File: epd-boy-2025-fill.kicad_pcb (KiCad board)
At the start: 2 copper layers, 33 x 64.5 mm, 43 parts, among them J1 FH12A-24S-0.5SH(55), Q1 SI1308EDL-T1-GE3, SW1 SW_Push, SW10 SW_SPDT, SW2 SW_Push, SW3 SW_Push, SW4 SW_Push, SW5 SW_Push, SW6 SW_Push, SW7 SW_Push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

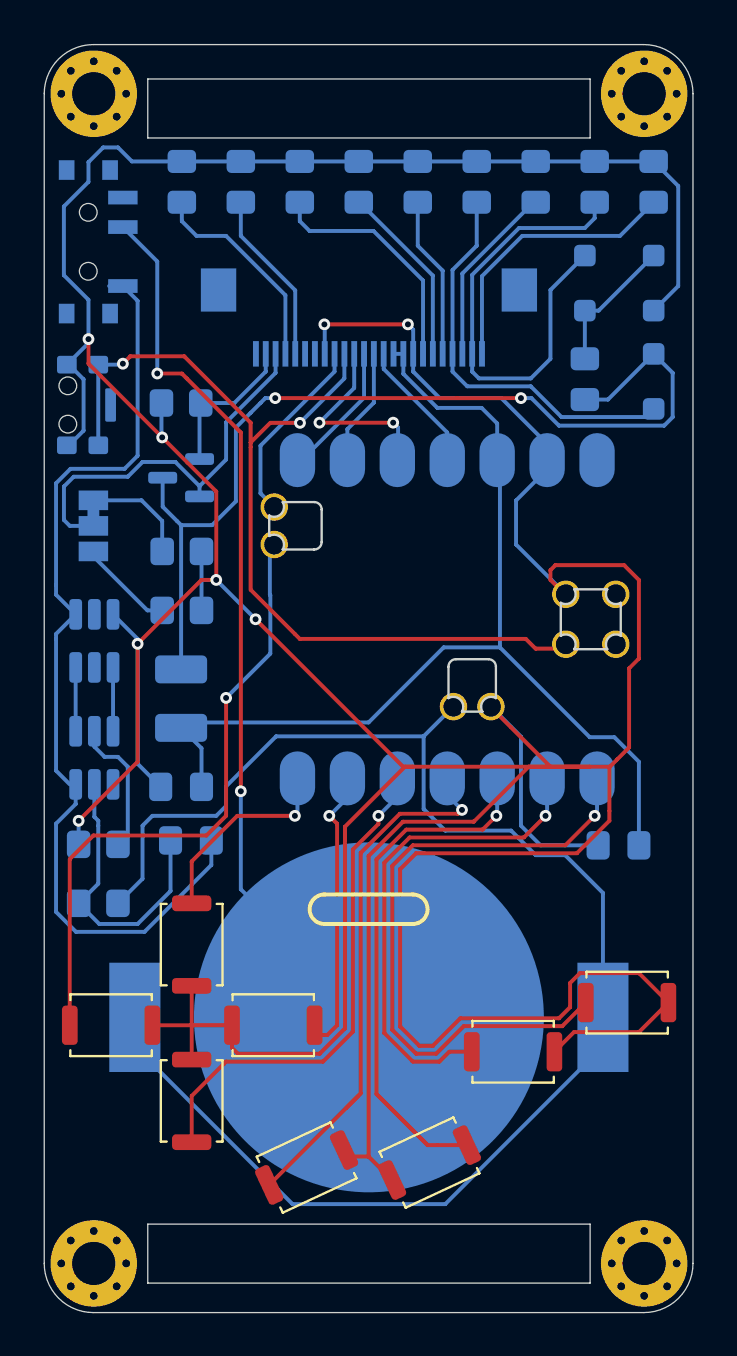
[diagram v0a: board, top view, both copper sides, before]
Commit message: Rerouted
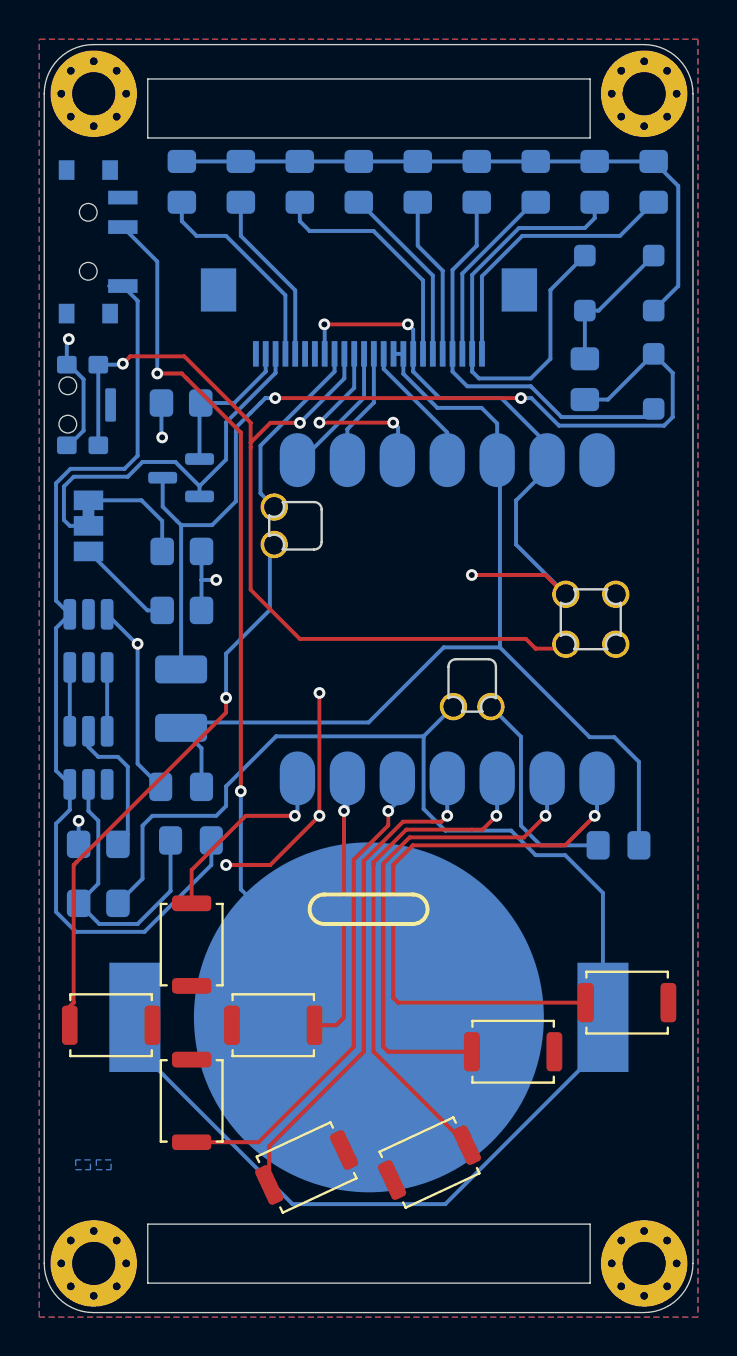
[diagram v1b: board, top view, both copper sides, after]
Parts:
- moved U2 0.30 mm to (102.0, 61.3)
- moved U3 0.30 mm to (102.0, 55.4)
- moved JP1 0.25 mm to (102.0, 49.5)
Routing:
- net GND: track 292.4 -> 109.1 mm, vias 8 -> 11
- net Net-(U1-A10/0.28): track 30.6 -> 26.0 mm
- net Net-(U1-NFC1/0.09_H): track 31.8 -> 28.5 mm
- net Net-(U1-A2/0.02_H): track 33.5 -> 30.9 mm
- net Net-(U1-A11/0.29): track 28.2 -> 26.0 mm
- net Net-(U1-A8_SDA/0.04_H): track 26.2 -> 25.3 mm
- added copper zone on B.Cu, net (none)
- added copper zone on B.Cu, net GND
- added copper zone on F.Cu, net GND
